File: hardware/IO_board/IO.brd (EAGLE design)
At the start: 167.9 x 122.5 mm, 69 parts, among them IC1 MAX232, IC10 74HCT245DW, IC11 74HCT393N, IC4 74HCT139N, IC5 74AC06N, IC7 MAX232, IC8 74HCT245DW, IC9 74HCT245DW, J1 DIN5, X2 CRYSTALS-NOGND-CFPX-217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

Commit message: CPU and I/O board update
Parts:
- removed IC11: 74HCT393N, 74xx-eu:DIL14
- removed JP1: (no value), pinhead:2X04
- removed QG1: (no value), crystal:DIL14S
- R1: device rcl:R0603 -> rcl:0204/7
- moved R1 130.1 mm to (139.7, 94.6), flipped to the top
- moved C31 59.2 mm to (-6.99, 101.6)
- moved C32 13.6 mm to (44.8, 59.5), turned to 270 degrees
- moved C16 5.12 mm to (141.6, 33.7), turned to 90 degrees
- moved C1 1.91 mm to (130.0, 69.2)
- moved C17 1.91 mm to (130.0, 54.0)
- moved C15 1.59 mm to (129.9, 84.5)
- moved IC10 1.27 mm to (137.8, 63.5)
- moved IC4 1.27 mm to (137.8, 22.2)
- moved IC8 1.27 mm to (137.8, 78.7)
- moved IC9 1.27 mm to (137.8, 48.3)
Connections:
- removed net 8275_DACK: SV2.2
- removed net BAUDRATE: IC2.13, IC2.14, JP1.2, JP1.4, JP1.6, JP1.8
- removed net BAUDRATE_153600: IC11.4
- removed net BAUDRATE_19200: IC11.11, JP1.1
- removed net BAUDRATE_2400: IC11.8, JP1.7
- removed net BAUDRATE_307200: IC11.3
- removed net BAUDRATE_38400: IC11.13, IC11.6
- removed net BAUDRATE_4800: IC11.9, JP1.5
- removed net BAUDRATE_76800: IC11.5
- removed net BAUDRATE_9600: IC11.10, IC2.27, JP1.3
- removed net N$26: IC11.1, QG1.8
- removed net N$30: QG1.1, R1.2
- removed net RDYIN: SV2.1
- new net BAUDRATE_A: IC2.13, IC2.14, IC6.8
- new net BAUDRATE_B: IC2.27, IC6.9
- new net BOARD_ENABLE: IC8.19
- new net IEI: IC2.6, SV2.1
- new net IEO: IC6.11, SV2.2
- new net TO0: IC6.7, R1.1
- net GND: no longer IC11.12, IC11.2, IC11.7, IC8.19, QG1.7
- net VCC: no longer IC11.14, QG1.14, R1.1
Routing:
- net IEI: track 0.00 -> 117.6 mm, vias 0 -> 2
- net IEO: track 0.00 -> 97.5 mm, vias 0 -> 2
- net BAUDRATE_A: track 0.00 -> 74.1 mm, vias 0 -> 4
- net TO0: track 0.00 -> 66.0 mm, vias 0 -> 2
- net BOARD_ENABLE: track 0.00 -> 51.5 mm, vias 0 -> 2
- net BAUDRATE_9600: track 45.1 -> 0.00 mm
- net VCC: track 656.3 -> 611.7 mm, vias 14 -> 16
- net BAUDRATE: track 39.0 -> 0.00 mm, vias 2 -> 0
- net BAUDRATE_B: track 0.00 -> 36.7 mm, vias 0 -> 2
- net GND: track 166.1 -> 200.4 mm, vias 22 -> 24
- net N$26: track 18.5 -> 0.00 mm
- net BAUDRATE_38400: track 16.3 -> 0.00 mm
- net CS_0: track 176.3 -> 170.4 mm
- net CLK: track 104.0 -> 107.8 mm
- net BAUDRATE_4800: track 3.18 -> 0.00 mm
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
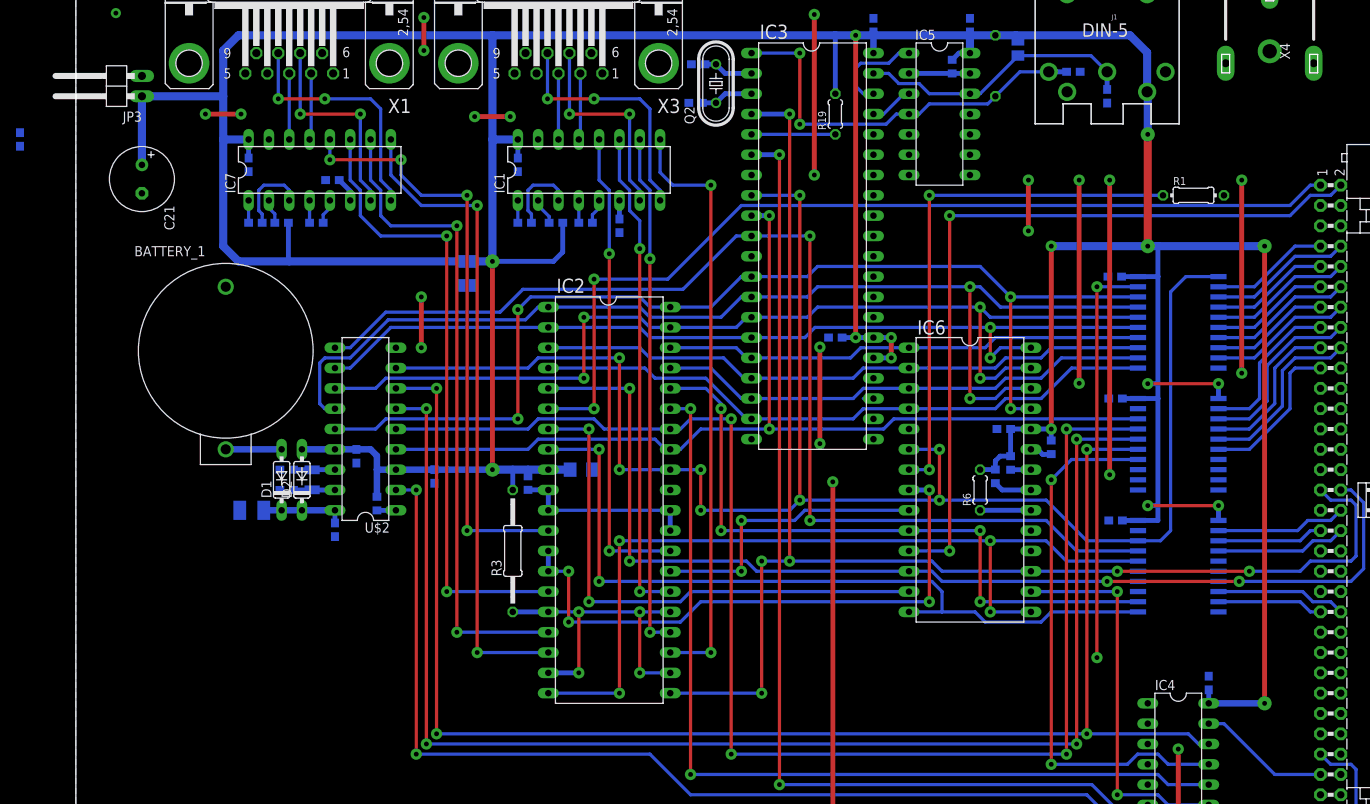
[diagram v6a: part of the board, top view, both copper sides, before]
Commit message: Audio circuit added to I/O board
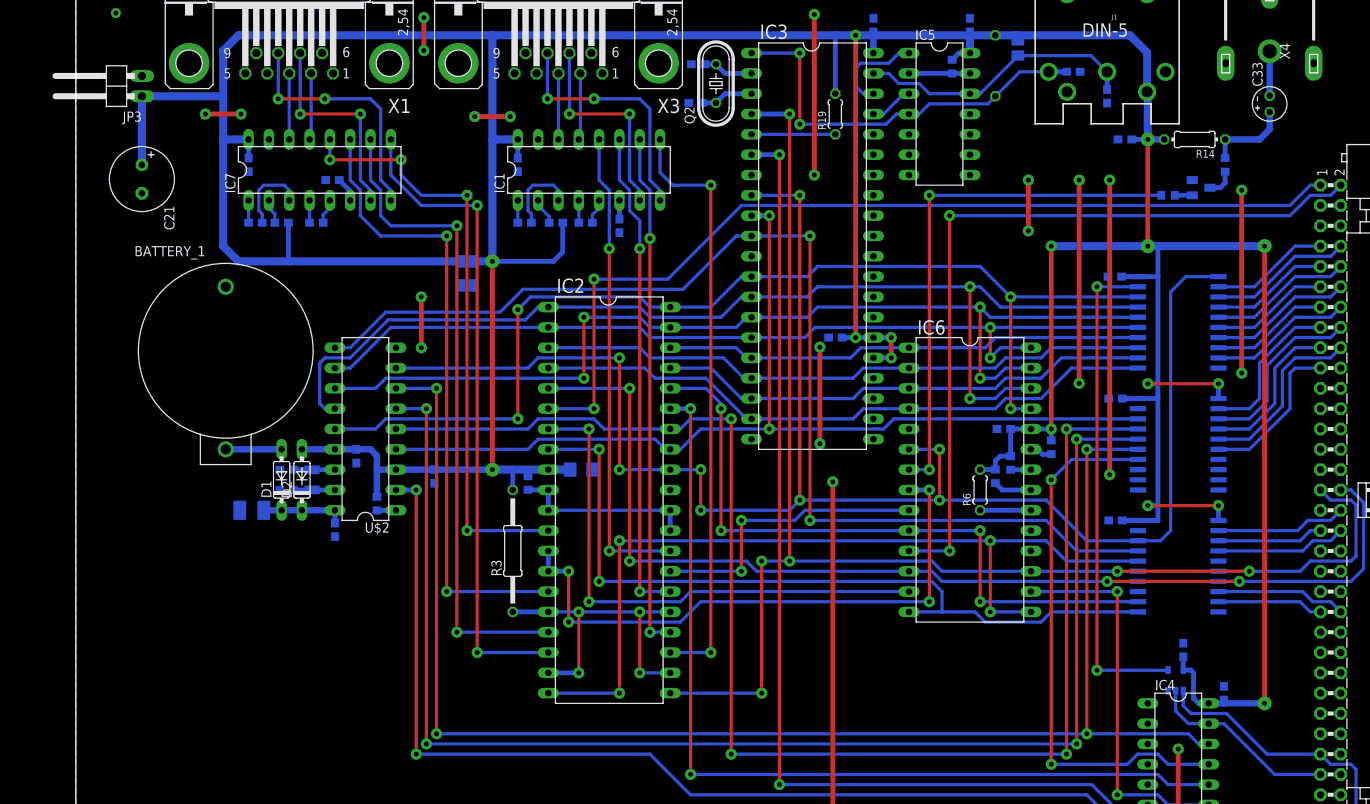
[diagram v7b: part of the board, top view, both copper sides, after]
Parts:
- added C33: (no value), rcl:E2-4
- added C34: 100N, rcl:C0603
- added IC11: 74LVC1G08DBV, 74xx-little-de:SOT23-5
- added R14: (no value), rcl:0204/7
- added R15: (no value), rcl:R0603
- added T1: BC847, transistor:SOT23
- R1: device rcl:0204/7 -> rcl:R0603
- moved C31 158.8 mm to (138.4, 37.8)
- moved R1 3.17 mm to (136.5, 94.6), flipped to the bottom, turned to 180 degrees
- moved C16 2.29 mm to (143.5, 32.4)
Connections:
- new net N$26: R1.2, T1.1
- new net N$27: R15.1, T1.3
- new net N$30: C33.-, X4.2
- new net N$40: C33.+, R14.1, R15.2
- net BOARD_ENABLE: now also IC11.4
- net CS_0: now also IC11.1
- net CS_2: now also IC11.2
- net GND: now also C34.2, IC11.3, T1.2, X4.1, X4.1@1, X4.1@2
- net VCC: now also C34.1, IC11.5, R14.2
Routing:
- net CS_0: track 170.4 -> 191.9 mm
- net VCC: track 611.7 -> 622.9 mm
- net N$40: track 0.00 -> 10.6 mm
- net BOARD_ENABLE: track 51.5 -> 62.0 mm
- net CS_2: track 16.6 -> 23.9 mm
- net N$30: track 0.00 -> 5.56 mm
- net N$27: track 0.00 -> 3.57 mm
- net N$26: track 0.00 -> 2.18 mm
- net GND: track 200.4 -> 199.1 mm

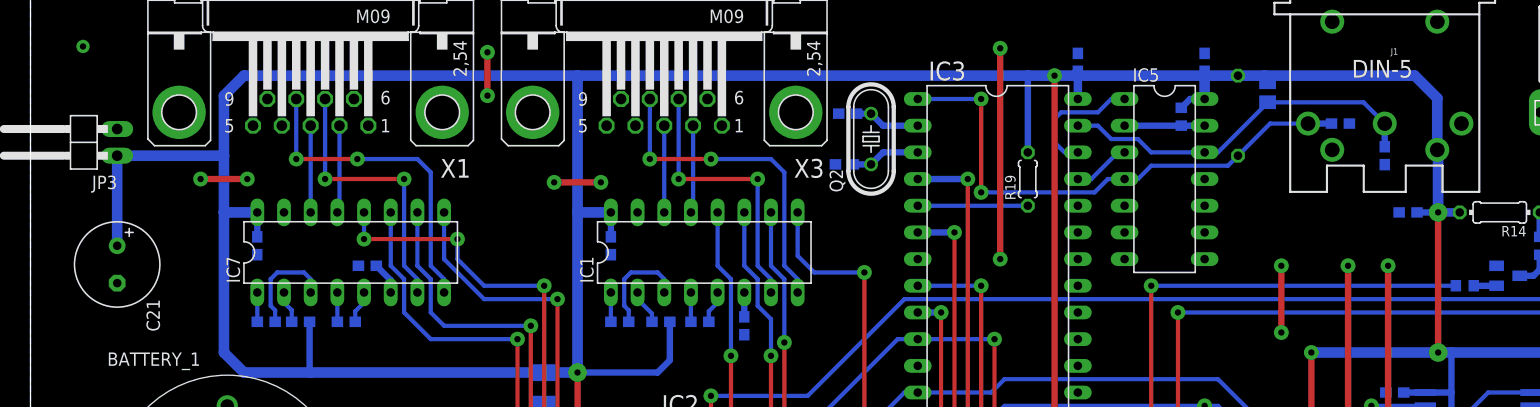
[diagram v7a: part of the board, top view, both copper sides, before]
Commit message: Capacitors added to I/O board
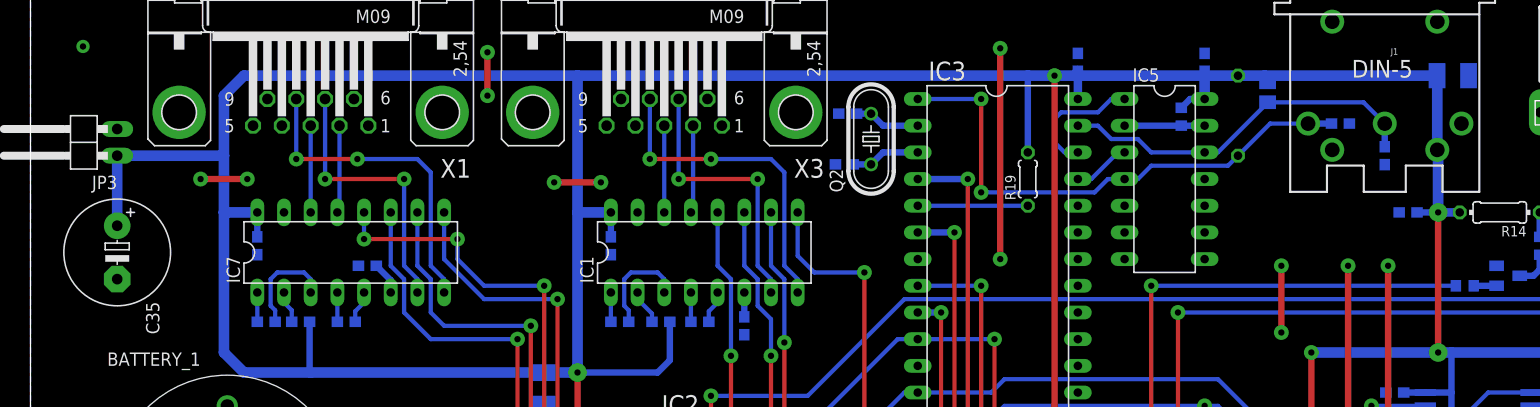
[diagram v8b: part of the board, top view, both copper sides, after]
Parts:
- added C35: (no value), rcl:E5-10,5
- C21: device rcl:E3,5-8 -> rcl:SMC_B
- moved C21 128.4 mm to (135.4, 114.6), flipped to the bottom, turned to 180 degrees
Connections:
- net GND: now also C35.-
- net VCC: now also C35.+
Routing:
- net VCC: track 622.9 -> 622.2 mm
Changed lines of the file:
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@@
 <setting verticaltext="up"/>
 </settings>
-<grid distance="25" unitdist="mil" unit="mil" style="lines" multiple="1" display="no" altdistance="12.5" altunitdist="mil" altunit="mil"/>
+<grid distance="25" unitdist="mil" unit="mil" style="lines" multiple="1" display="no" altdistance="1" altunitdist="mil" altunit="mil"/>
 <layers>
 <layer number="1" name="Top" color="4" fill="1" visible="yes" active="yes"/>
@@
 <element name="C19" library="rcl" package="C0603" value="100N" x="115.9891" y="65.405" rot="MR0"/>
 <element name="JP3" library="pinhead" package="1X02/90" value="" x="4.445" y="108.2675" rot="R90"/>
-<element name="C21" library="rcl" package="E3,5-8" value="" x="8.255" y="96.647" rot="R270"/>
 <element name="C24" library="rcl" package="SMC_B" value="" x="48.895" y="84.8487" rot="MR270"/>
 <element name="IC4" library="74xx-eu" package="DIL16" value="74HCT139N" x="137.795" y="22.225" rot="R270"/>
@@
 <element name="R15" library="rcl" package="R0603" value="" x="143.6575" y="98.425" rot="MR90"/>
 <element name="C34" library="rcl" package="C0603" value="100N" x="131.1275" y="101.6" rot="MR0"/>
+<element name="C35" library="rcl" package="E5-10,5" value="" x="8.255" y="97.79" rot="R270"/>
+<element name="C21" library="rcl" package="SMC_B" value="" x="135.382" y="114.6175" rot="MR180"/>
 </elements>
 <signals>
@@
 <contactref element="C19" pad="2"/>
 <contactref element="JP3" pad="2"/>
-<contactref element="C21" pad="-"/>
 <contactref element="C24" pad="-"/>
 <contactref element="IC4" pad="8"/>
@@
 <contactref element="X4" pad="1@1"/>
 <contactref element="C34" pad="2"/>
+<contactref element="C35" pad="-"/>
+<contactref element="C21" pad="-"/>
 </signal>
 <signal name="N$37">
@@
 <wire x1="97.4725" y1="76.835" x2="97.4725" y2="114.6175" width="0.6096" layer="1"/>
 <wire x1="133.985" y1="107.475" x2="133.905" y2="107.555" width="0.6096" layer="16"/>
-<wire x1="133.905" y1="107.555" x2="133.905" y2="112.475" width="1.016" layer="16"/>
+<wire x1="133.905" y1="107.555" x2="133.905" y2="114.5945" width="1.016" layer="16"/>
 <via x="97.4725" y="114.6175" extent="1-16" drill="0.6" diameter="1.4224" shape="octagon"/>
 <wire x1="99.695" y1="114.6175" x2="97.4725" y2="114.6175" width="1.016" layer="16"/>
@@
 <wire x1="94.9325" y1="114.6175" x2="52.07" y2="114.6175" width="1.016" layer="16"/>
 <wire x1="52.07" y1="114.6175" x2="20.32" y2="114.6175" width="1.016" layer="16"/>
-<contactref element="C21" pad="+"/>
 <contactref element="C24" pad="+"/>
 <contactref element="IC3" pad="25"/>
@@
 <wire x1="111.76" y1="114.6175" x2="114.935" y2="114.6175" width="1.016" layer="16"/>
 <wire x1="114.935" y1="114.6175" x2="117.475" y2="114.6175" width="1.016" layer="16"/>
-<wire x1="117.475" y1="114.6175" x2="131.7625" y2="114.6175" width="1.016" layer="16"/>
-<wire x1="131.7625" y1="114.6175" x2="133.905" y2="112.475" width="1.016" layer="16"/>
+<wire x1="117.475" y1="114.6175" x2="133.882" y2="114.6175" width="1.016" layer="16"/>
 <wire x1="111.76" y1="112.395" x2="111.76" y2="114.6175" width="1.016" layer="16"/>
 <wire x1="111.76" y1="114.6175" x2="111.76" y2="115.0375" width="0.4064" layer="16"/>
@@
 <contactref element="C31" pad="1"/>
 <contactref element="C32" pad="1"/>
-<wire x1="8.255" y1="98.425" x2="8.255" y2="106.9975" width="1.016" layer="16"/>
 <contactref element="R2" pad="2"/>
 <wire x1="56.515" y1="59.4986" x2="56.515" y2="60.325" width="0.4064" layer="16"/>
@@
 <contactref element="C34" pad="1"/>
 <wire x1="131.9775" y1="101.6" x2="133.985" y2="101.6" width="0.6096" layer="16"/>
+<contactref element="C35" pad="+"/>
+<wire x1="8.255" y1="106.9975" x2="8.255" y2="100.33" width="1.016" layer="16"/>
+<contactref element="C21" pad="+"/>
+<wire x1="133.905" y1="114.5945" x2="133.882" y2="114.6175" width="1.016" layer="16"/>
 </signal>
 <signal name="INT">
